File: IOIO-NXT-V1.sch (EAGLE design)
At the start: 14 parts

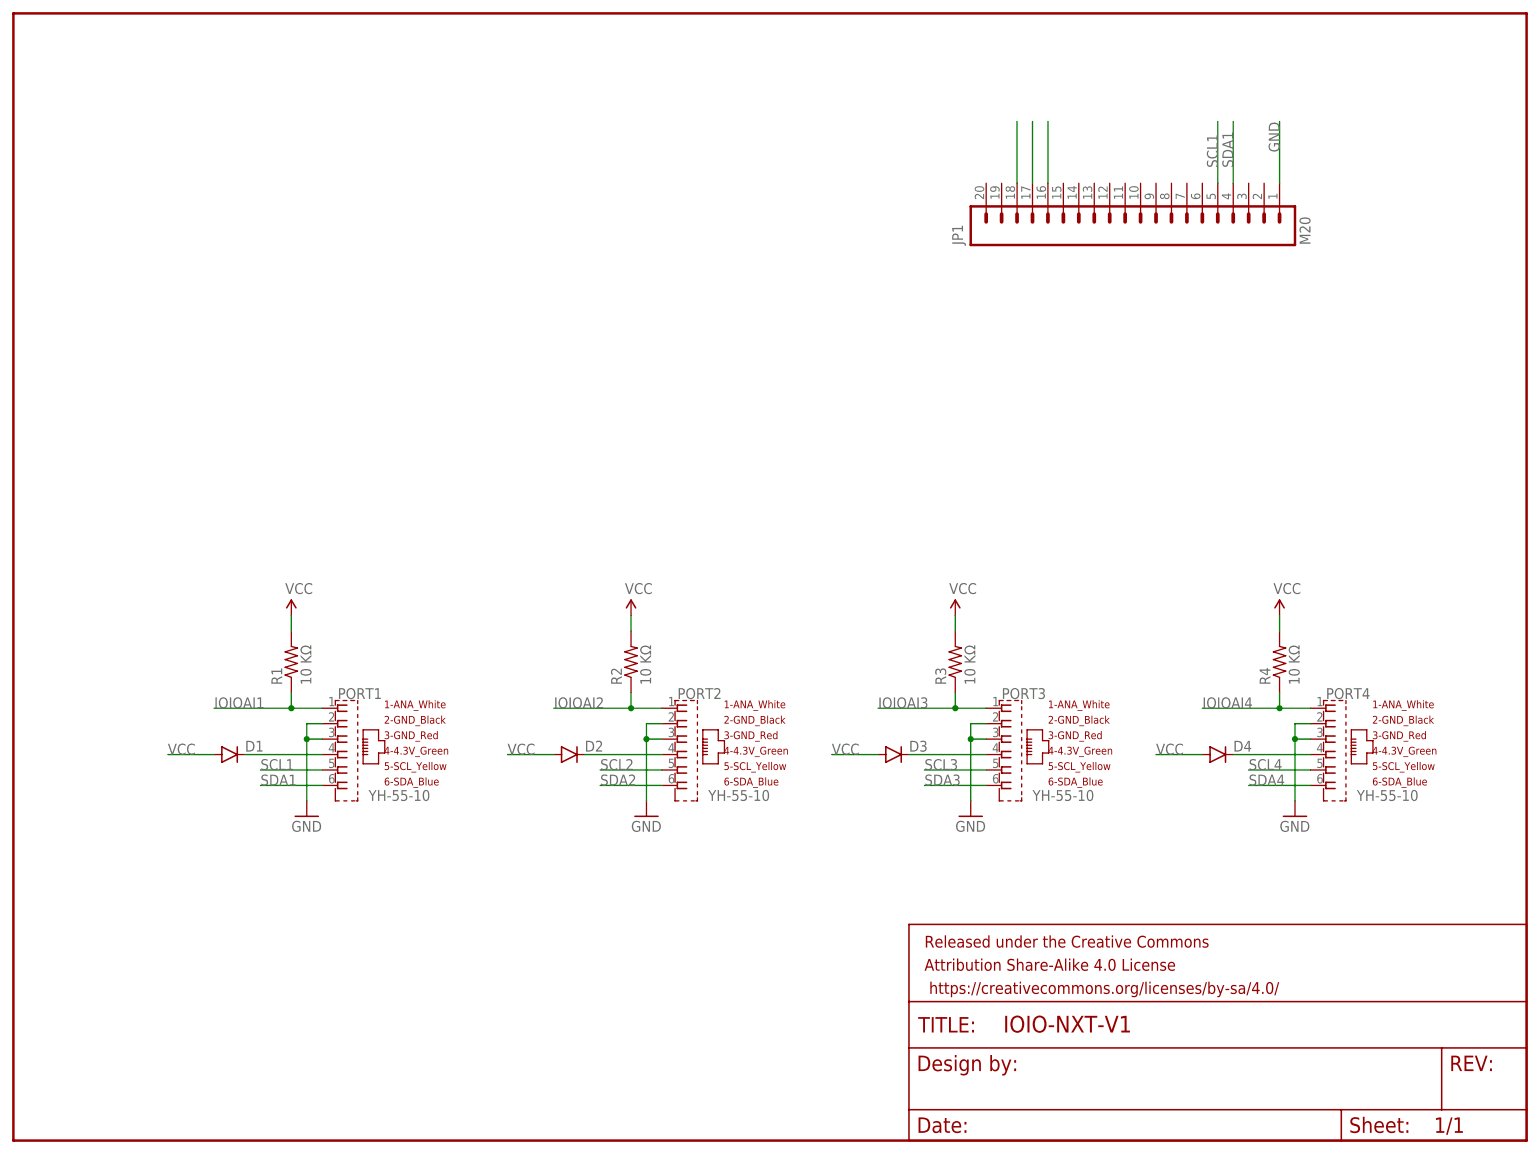
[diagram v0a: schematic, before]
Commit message: Added IOIO headers and EA logo.  Waiting for analog pin #s
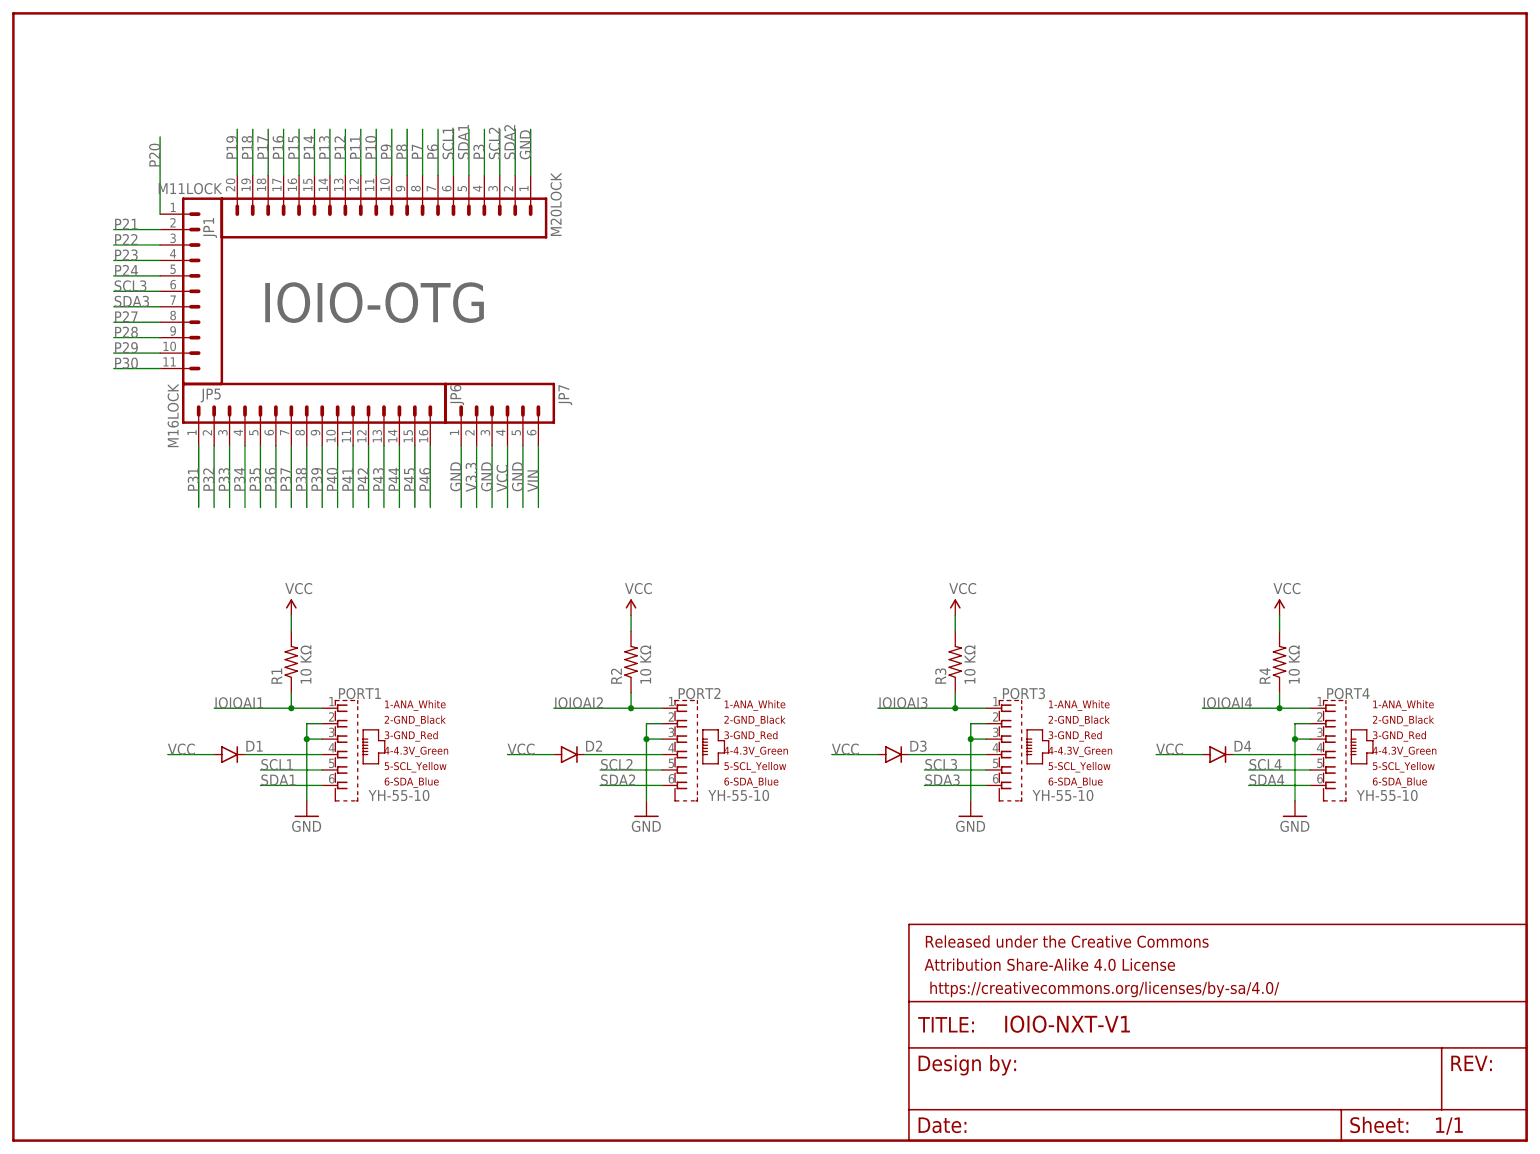
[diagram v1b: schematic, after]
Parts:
- added JP5: M11LOCK, SparkFun-Connectors:M11LOCK
- added JP6: M16LOCK, SparkFun-Connectors:M16LOCK
- added JP7: (no value), SparkFun-Connectors:M06LOCK
- JP1: value M20 -> M20LOCK; device SparkFun-Connectors:M20 -> SparkFun-Connectors:M20LOCK
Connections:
- new net P10: JP1.11
- new net P11: JP1.12
- new net P12: JP1.13
- new net P13: JP1.14
- new net P14: JP1.15
- new net P15: JP1.16
- new net P16: JP1.17
- new net P17: JP1.18
- new net P18: JP1.19
- new net P19: JP1.20
- new net P20: JP5.1
- new net P21: JP5.2
- new net P22: JP5.3
- new net P23: JP5.4
- new net P24: JP5.5
- new net P27: JP5.8
- new net P28: JP5.9
- new net P29: JP5.10
- new net P3: JP1.4
- new net P30: JP5.11
- new net P31: JP6.1
- new net P32: JP6.2
- new net P33: JP6.3
- new net P34: JP6.4
- new net P35: JP6.5
- new net P36: JP6.6
- new net P37: JP6.7
- new net P38: JP6.8
- new net P39: JP6.9
- new net P40: JP6.10
- new net P41: JP6.11
- new net P42: JP6.12
- new net P43: JP6.13
- new net P44: JP6.14
- new net P45: JP6.15
- new net P46: JP6.16
- new net P6: JP1.7
- new net P7: JP1.8
- new net P8: JP1.9
- new net P9: JP1.10
- new net V3.3: JP7.2
- new net VIN: JP7.6
- net GND: now also JP7.1, JP7.3, JP7.5
- net SCL1: now also JP1.6; no longer JP1.5
- net SCL2: now also JP1.3
- net SCL3: now also JP5.6
- net SDA1: now also JP1.5; no longer JP1.4
- net SDA2: now also JP1.2; no longer JP1.16
- net SDA3: now also JP5.7; no longer JP1.17
- net SDA4: no longer JP1.18
- net VCC: now also JP7.4
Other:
- note added: "IOIO-OTG"
- moved on the sheet: JP1
